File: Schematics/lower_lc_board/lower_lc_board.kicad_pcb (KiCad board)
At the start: 4 copper layers, 69.5 x 60 mm, 179 parts, among them J1 Stack Male Edge Connector, J10 SOL_CONN, J11 Screw_Terminal_01x02, J2 SWD_CONN, J3 USB_C_CONN, J4 HALL-1, J5 HALL-2, J6 PT1, J7 Screw_Terminal_01x02, J8 PT1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

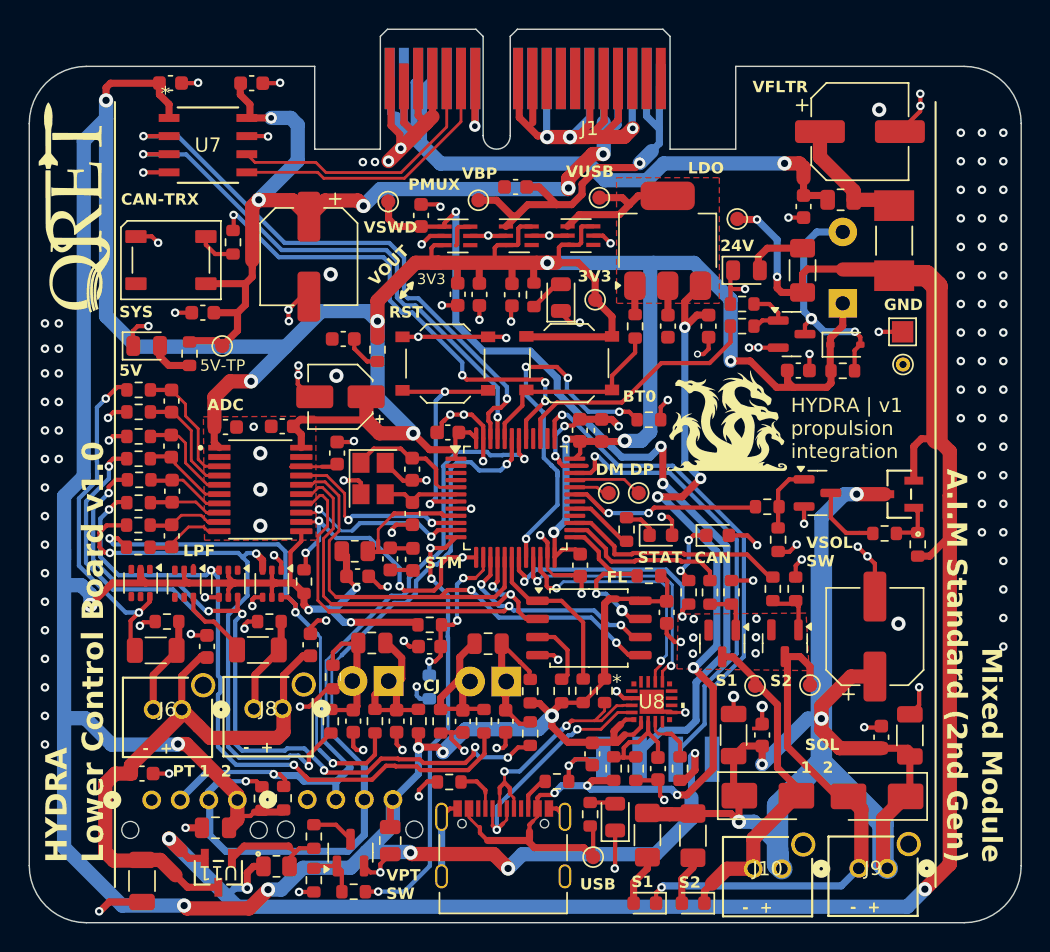
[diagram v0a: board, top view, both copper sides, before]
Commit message: new backplane connector
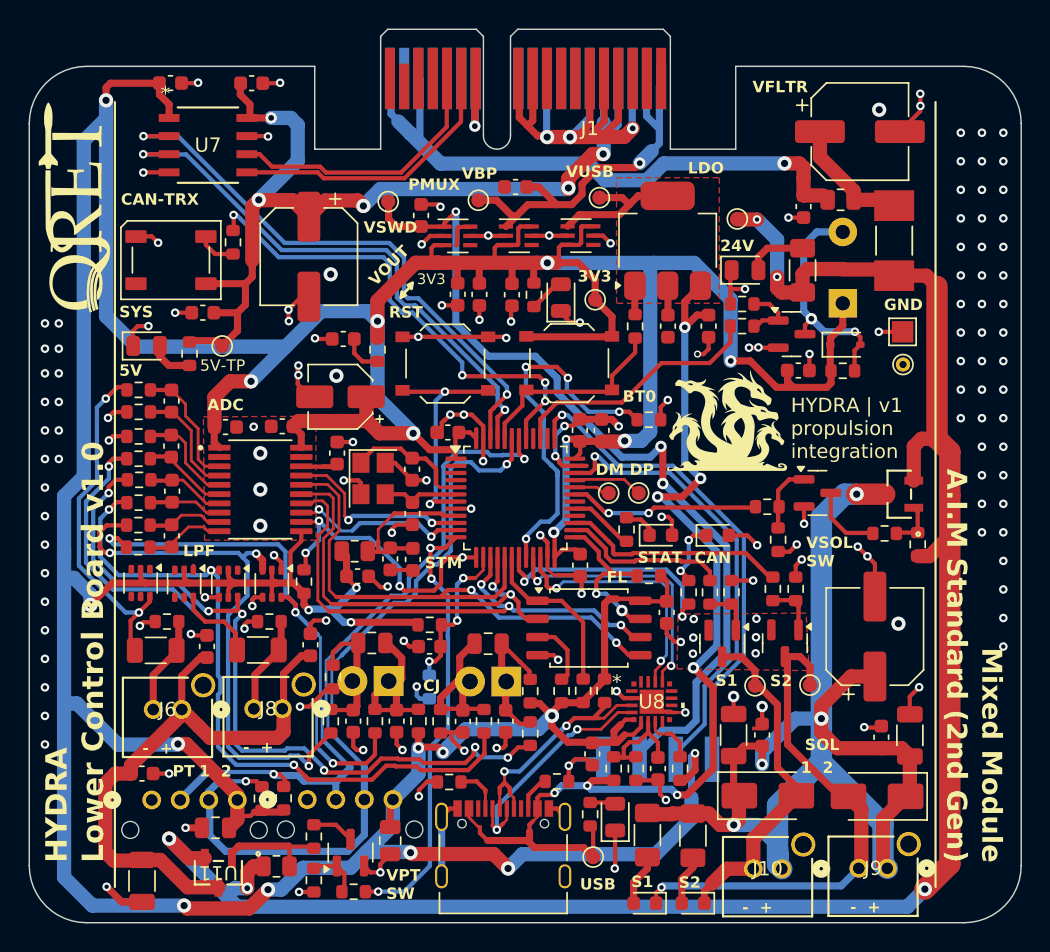
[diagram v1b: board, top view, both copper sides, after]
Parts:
- moved D2 0.10 mm to (170.8, 61.8)
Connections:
- J1 pad A15: +24V_BP -> unconnected-(J1-Reserved-PadA15)
- J1 pad A17: +24V_BP -> unconnected-(J1-Reserved-PadA17)
- J1 pad B15: GND -> unconnected-(J1-Reserved-PadB15)
- J1 pad B16: GND -> unconnected-(J1-Reserved-PadB16)
- J1 pad B17: GND -> unconnected-(J1-Reserved-PadB17)
- J1 pad B18: GND -> unconnected-(J1-Reserved-PadB18)
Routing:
- net GND: track 243.5 -> 226.0 mm, vias 175 -> 172
- net +24V_BP: track 51.0 -> 42.9 mm
- net +3V3: track 422.4 -> 424.8 mm
- net Net-(U9-CAP): track 3.54 -> 2.79 mm
- net SPI_SCLK: track 38.4 -> 37.9 mm

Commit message: review changes
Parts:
- moved D4 0.15 mm to (161.8, 100.1), turned to -90 degrees
- moved R4 0.15 mm to (160.1, 99.9), turned to -90 degrees
- moved R30 0.14 mm to (164.1, 101.4)
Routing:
- net +3V3: track 424.8 -> 415.1 mm
- net 5V_USB: track 74.2 -> 75.0 mm, vias 7 -> 6
- net GND: vias 172 -> 171

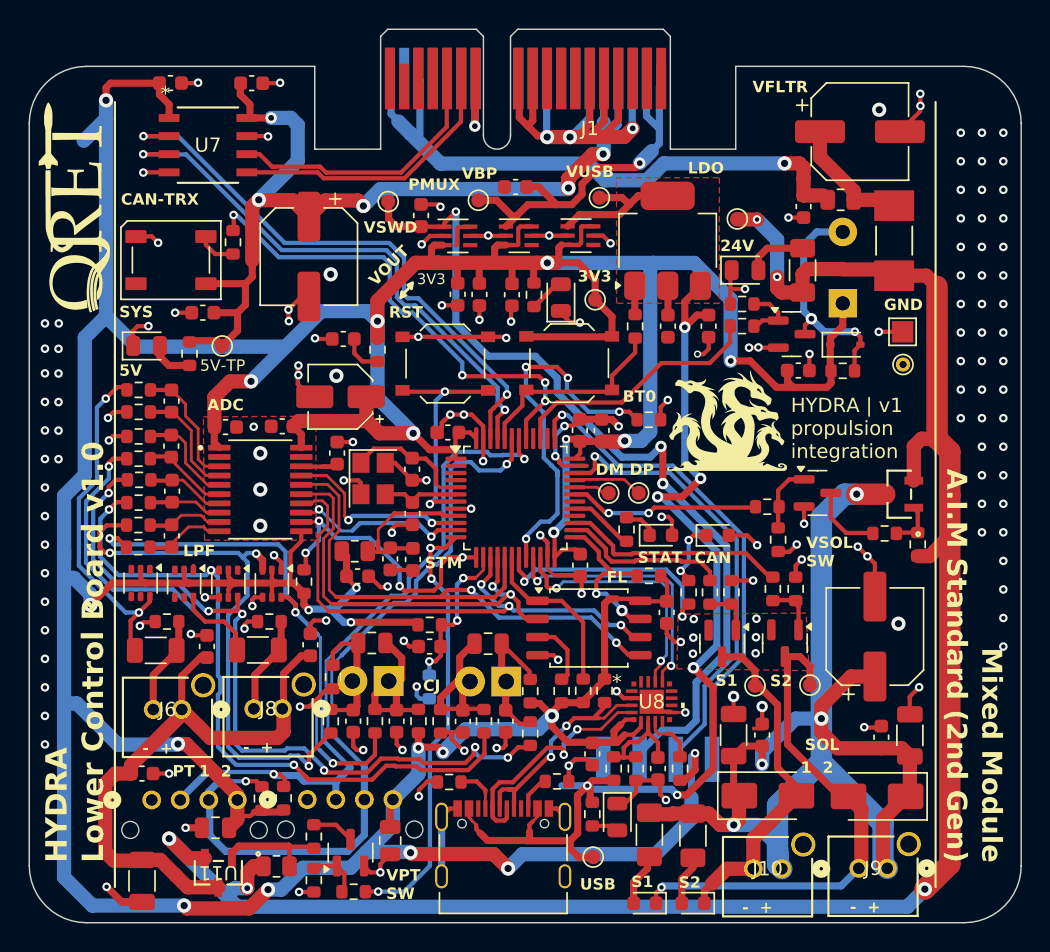
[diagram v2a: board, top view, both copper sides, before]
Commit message: start of review for lower control board, Cleaning up power and spi traces
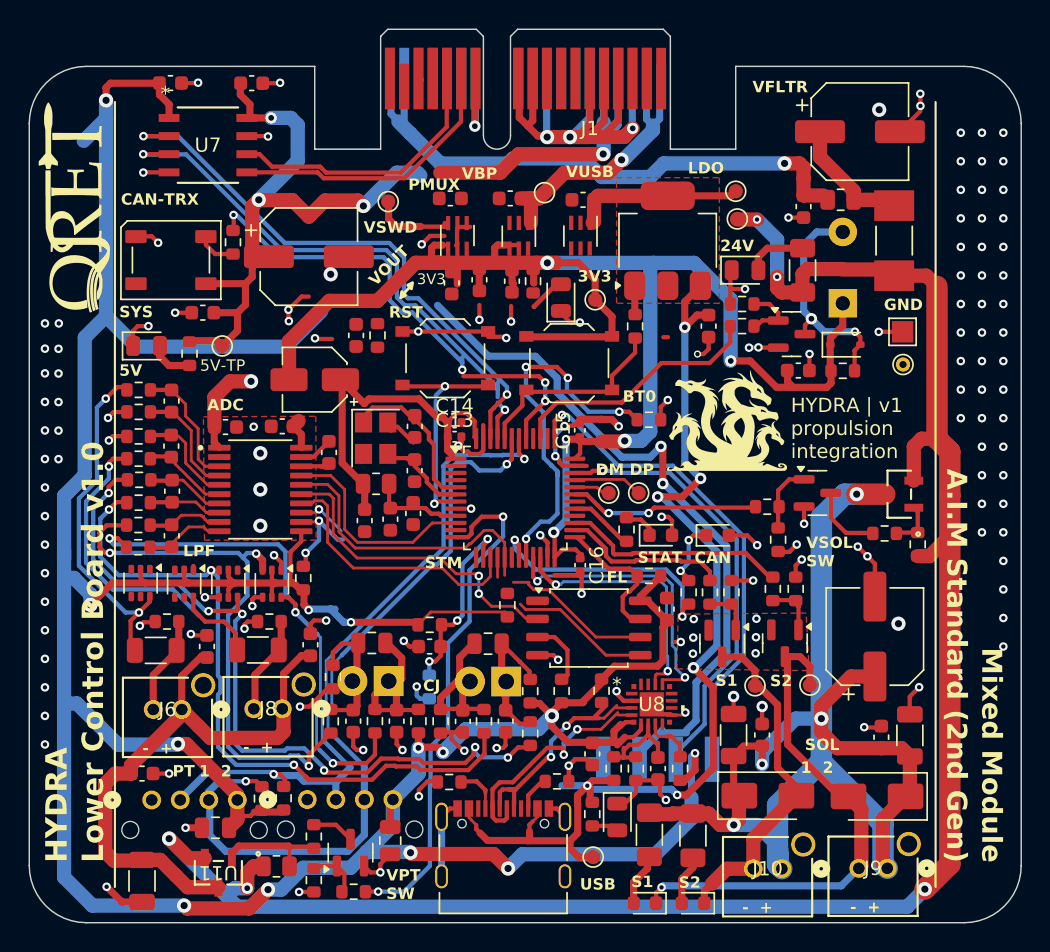
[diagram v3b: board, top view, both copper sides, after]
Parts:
- removed ?: , 
- C13, C14, C15, C16: footprint Capacitor_SMD:C_0603_1608Metric -> Capacitor_SMD:C_0402_1005Metric
- moved C6 10.7 mm to (159.4, 56.9), turned to 180 degrees
- moved C14 10.3 mm to (150.4, 72.5), turned to 0 degrees
- moved TP6 9.56 mm to (170.1, 56.3)
- moved R48 8.01 mm to (154.1, 85.3)
- moved FB2 4.95 mm to (144.9, 76.8)
- moved TP4 4.66 mm to (156.7, 56.4)
- moved C49 3.94 mm to (144.1, 79.4), turned to -90 degrees
- moved C48 3.57 mm to (147.5, 78.9)
- moved C45 3.23 mm to (145.9, 79.3)
- moved C11 3.01 mm to (147.6, 75.9)
- moved C10 3.01 mm to (147.6, 72.8)
- moved Y1 2.84 mm to (144.9, 73.6)
- moved C44 2.37 mm to (150.1, 56.8), turned to 180 degrees
- moved C12 2.16 mm to (140.6, 69.5)
- moved C52 1.03 mm to (152.1, 62.5)
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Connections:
- J1 pad A16: +24V_BP -> unconnected-(J1-Reserved-PadA16)
- J1 pad A17: unconnected-(J1-Reserved-PadA17) -> +24V_BP
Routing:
- net GND: track 226.0 -> 201.9 mm, vias 171 -> 156
- net ADC_CS: track 20.7 -> 7.33 mm, vias 4 -> 2
- net FL_CS: track 11.9 -> 0.00 mm
- net SPI_MOSI: track 41.0 -> 30.7 mm, vias 2 -> 0
- net ADC_DRDY: track 12.4 -> 3.51 mm, vias 2 -> 1
- net SPI_SCLK: track 37.9 -> 29.4 mm, vias 3 -> 0
- net /Power Circuitry/3V3_BP: track 26.9 -> 19.7 mm
- net V_SWD: track 61.3 -> 54.2 mm, vias 3 -> 2
- net +3V3: track 415.1 -> 408.9 mm, vias 22 -> 19
- net SPI_MISO: track 29.9 -> 24.1 mm
- net VPT-SW: track 30.9 -> 36.3 mm, vias 3 -> 2
- net +3.3VA: track 10.8 -> 6.56 mm
- net STM_RESET: track 19.1 -> 15.7 mm
- net OSC_IN: track 8.86 -> 11.4 mm
- net TEMP_SENSE: track 11.7 -> 14.0 mm
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
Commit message: review work
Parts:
- moved C44 4.92 mm to (145.3, 58.0), turned to -90 degrees
- moved TP9 4.04 mm to (149.8, 57.4)
- moved U10 3.41 mm to (147.4, 58.2), turned to -90 degrees
- moved C5 3.00 mm to (151.6, 58.0), turned to 90 degrees
- moved C6 1.96 mm to (157.8, 58.0), turned to -90 degrees
- moved U3 1.73 mm to (153.6, 58.2)
- moved C9 1.57 mm to (145.1, 66.4)
- moved R6 1.43 mm to (143.6, 66.4)
- moved U4 1.33 mm to (159.9, 58.2)
- moved TP4 1.25 mm to (156.0, 57.4)
- moved C51 0.90 mm to (150.3, 61.8)
- moved R1 0.81 mm to (155.6, 61.8)
- moved C50 0.81 mm to (154.2, 61.8)
- moved C52 0.72 mm to (151.8, 61.8)
- moved C16 0.64 mm to (158.9, 81.9)
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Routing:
- net GND: track 201.9 -> 228.5 mm, vias 156 -> 172
- net ADC_CS: track 7.33 -> 19.9 mm, vias 2 -> 3
- net ADC_DRDY: track 3.51 -> 15.4 mm, vias 1 -> 2
- net V_SWD: track 54.2 -> 63.8 mm, vias 2 -> 3
- net /Power Circuitry/3V3_BP: track 19.7 -> 26.6 mm
- net STM_RESET: track 15.7 -> 21.9 mm
- net SPI_MISO: track 24.1 -> 29.4 mm, vias 2 -> 3
- net FL_CS: track 0.00 -> 4.98 mm
- net SPI_MOSI: track 30.7 -> 34.8 mm, vias 0 -> 3
- net SPI_SCLK: track 29.4 -> 25.3 mm, vias 0 -> 1
- net /Power Circuitry/3V3_USB: track 11.9 -> 9.32 mm
- net /Valve Control Circuitry/VSOL: track 89.8 -> 88.0 mm
- net ADC_CLKIN: track 15.0 -> 16.5 mm
- net TEMP_SENSE: track 14.0 -> 15.5 mm
- net CAN_P: track 19.3 -> 17.8 mm
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- added copper zone on B.Cu, net GND
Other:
- board text removed: "STM"

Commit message: cleanup
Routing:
- net SPI_SCLK: track 25.3 -> 33.3 mm, vias 1 -> 2
- net HALL_SDA: track 54.9 -> 57.6 mm
- net GND: track 228.5 -> 230.5 mm, vias 172 -> 210
- net SPI_MOSI: track 34.8 -> 34.3 mm
- net +3V3: track 409.1 -> 409.0 mm, vias 21 -> 19
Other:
- board text removed: "5V-TP"

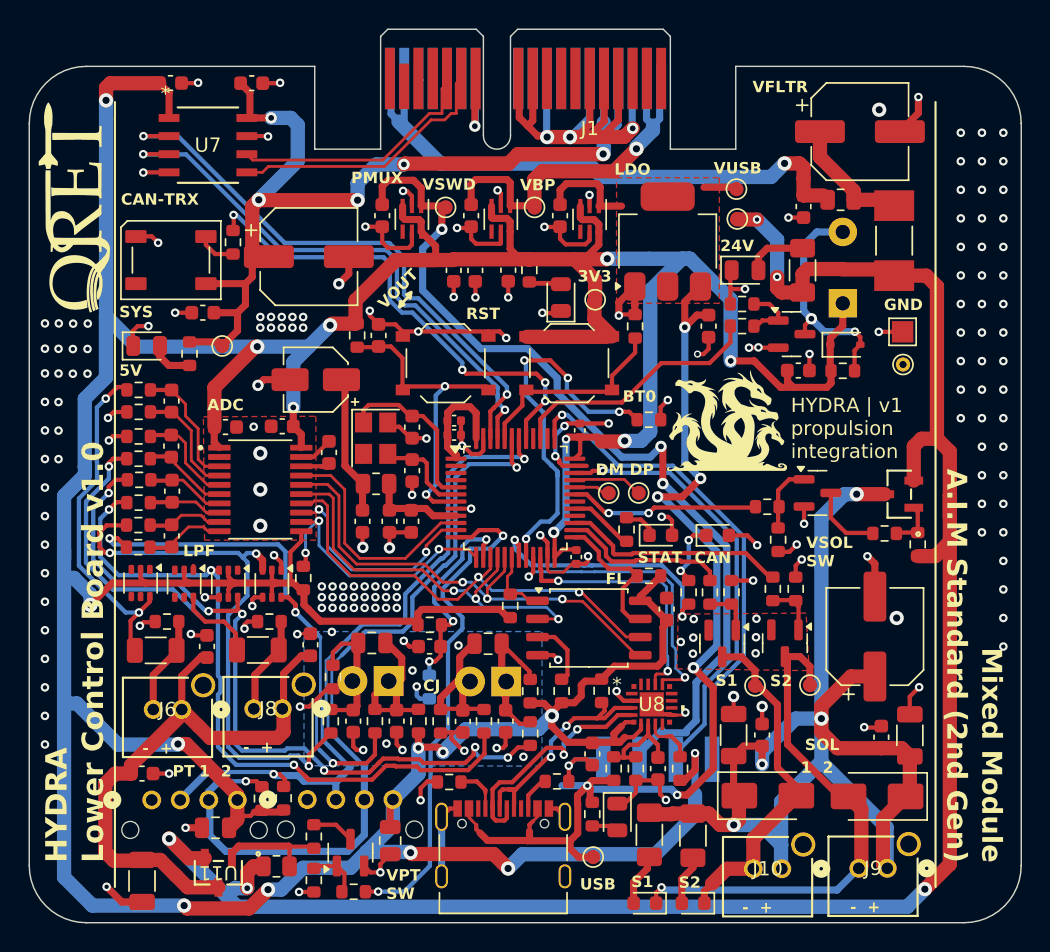
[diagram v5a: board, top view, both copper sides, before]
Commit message: add gnd pour
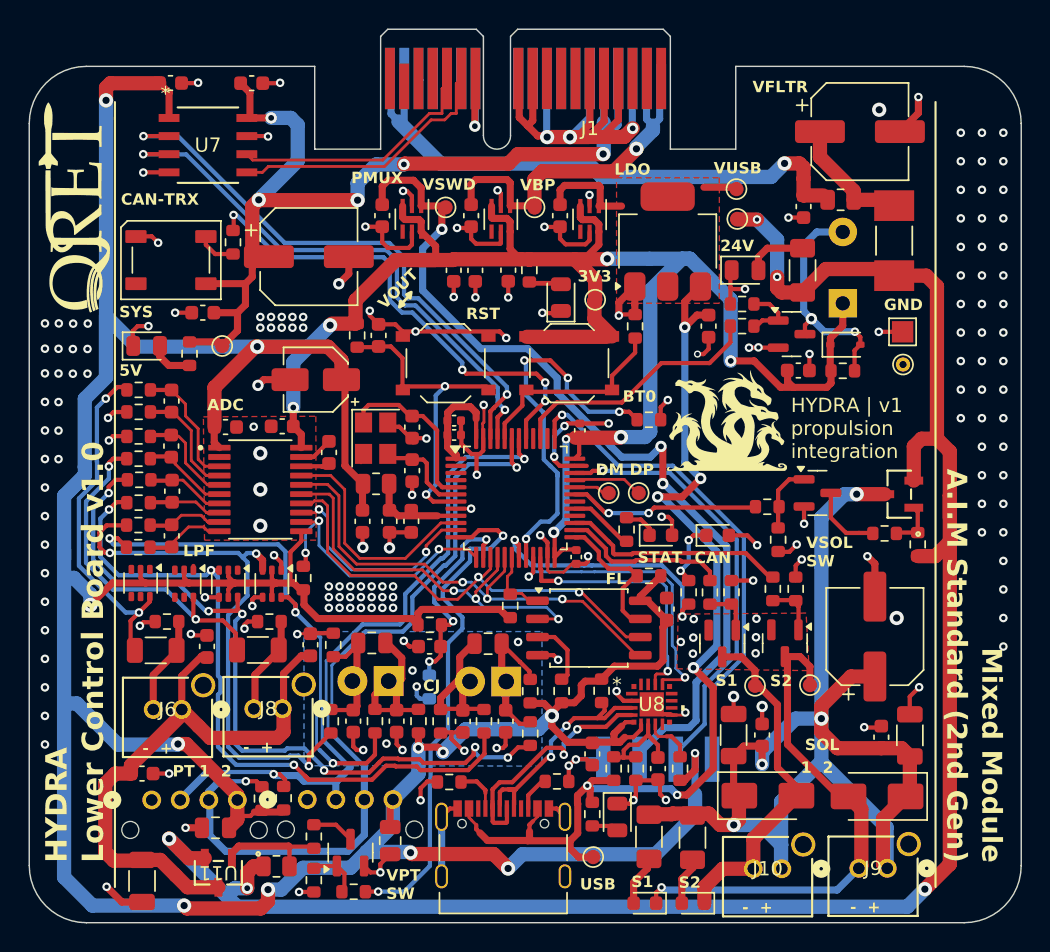
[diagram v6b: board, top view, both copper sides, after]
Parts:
- moved R27 2.25 mm to (141.9, 88.1), turned to 90 degrees
- moved R30 0.14 mm to (164.0, 101.5)
- moved R31 0.14 mm to (167.1, 101.6)
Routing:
- net +3V3: track 409.0 -> 416.5 mm
- net GND: track 230.5 -> 234.7 mm, vias 210 -> 207
- net 5V_USB: track 75.0 -> 73.2 mm
- net /Sensing Circuitry/TC_N_1: track 9.54 -> 8.72 mm
- net +24V: track 136.1 -> 135.4 mm
- net Net-(D14A-K3A4): track 24.2 -> 24.4 mm, vias 1 -> 2
- added copper zone on In1.Cu, net GND
- added copper zone on In2.Cu, net GND

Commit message: pmux fix
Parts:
- moved C44 4.34 mm to (149.7, 58.0)
- moved C5 4.16 mm to (155.7, 58.0)
- moved C6 3.16 mm to (160.9, 57.6)
- moved TP4 2.13 mm to (155.7, 55.3)
- moved TP9 2.03 mm to (149.7, 55.4)
- moved U4 1.11 mm to (158.8, 57.8)
- moved U3 0.51 mm to (153.4, 57.8)
- moved U10 0.36 mm to (147.5, 57.9)
- moved C4 0.29 mm to (140.5, 60.9)
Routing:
- net +3V3: track 416.5 -> 431.5 mm, vias 19 -> 21
- net /Power Circuitry/3V3_BP: track 26.3 -> 19.9 mm
- net /Power Circuitry/3V3_USB: track 9.22 -> 5.22 mm
- net V_SWD: track 63.8 -> 62.0 mm
- net +5V: track 67.1 -> 67.7 mm
- net GND: track 234.7 -> 234.5 mm, vias 207 -> 204
